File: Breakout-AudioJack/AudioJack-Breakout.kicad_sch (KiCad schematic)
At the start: 3 parts, among them J3 AudioJack2_Ground, J4 Conn_01x02, J8 Conn_01x02

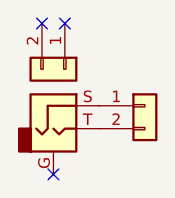
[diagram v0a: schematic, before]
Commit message: Update AudioJack breakout board post fabrication issues
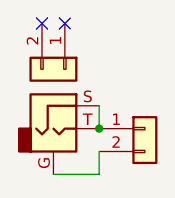
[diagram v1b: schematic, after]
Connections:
- net at J3.S, J4.1 (Pin_1): now also J3.T
- net at J4.2 (Pin_2): now also J3.G; no longer J3.T
- no-connect marks 3 -> 2
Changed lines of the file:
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@@
 (kicad_sch (version 20211123) (generator eeschema)
   (paper "A4")
+  (junction (at 114.046 67.056) (diameter 0) (color 0 0 0 0)
+  )
   (no_connect (at 110.236 55.372))
-  (no_connect (at 108.966 72.136))
   (no_connect (at 107.696 55.372))
-  (symbol (lib_id "Connector_Generic:Conn_01x02") (at 119.126 64.516 0) (unit 1)
+  (wire (pts (xy 114.046 69.596) (xy 114.046 72.136))
+    (stroke (width 0) (type default) (color 0 0 0 0))
+  )
+  (wire (pts (xy 114.046 64.516) (xy 114.046 67.056))
+    (stroke (width 0) (type default) (color 0 0 0 0))
+  )
+  (wire (pts (xy 114.046 72.136) (xy 108.966 72.136))
+    (stroke (width 0) (type default) (color 0 0 0 0))
+  )
+  (symbol (lib_id "Connector_Generic:Conn_01x02") (at 119.126 67.056 0) (unit 1)
     (in_bom yes) (on_board yes) (fields_autoplaced)
-    (property "Reference" "J4" (id 0) (at 117.8559 61.722 90)
+    (property "Reference" "J4" (id 0) (at 117.8559 64.262 90)
       (effects (font (size 1.27 1.27)) (justify left) hide)
     )
-    (property "Value" "Conn_01x02" (id 1) (at 120.3959 61.722 90)
+    (property "Value" "Conn_01x02" (id 1) (at 120.3959 64.262 90)
       (effects (font (size 1.27 1.27)) (justify left) hide)
     )
-    (property "Footprint" "Connector_PinHeader_2.54mm:PinHeader_1x02_P2.54mm_Vertical" (id 2) (at 119.126 64.516 0)
+    (property "Footprint" "Connector_PinHeader_2.54mm:PinHeader_1x02_P2.54mm_Vertical" (id 2) (at 119.126 67.056 0)
       (effects (font (size 1.27 1.27)) hide)
     )
-    (property "Datasheet" "~" (id 3) (at 119.126 64.516 0)
+    (property "Datasheet" "~" (id 3) (at 119.126 67.056 0)
       (effects (font (size 1.27 1.27)) hide)
     )
